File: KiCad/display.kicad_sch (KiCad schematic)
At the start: 36 parts, among them IC2 R1200N001A-TR-FE, J3 Conn_01x34_NHD_18, Q3 DMG2302U, U6 LT1963AxST-2.5

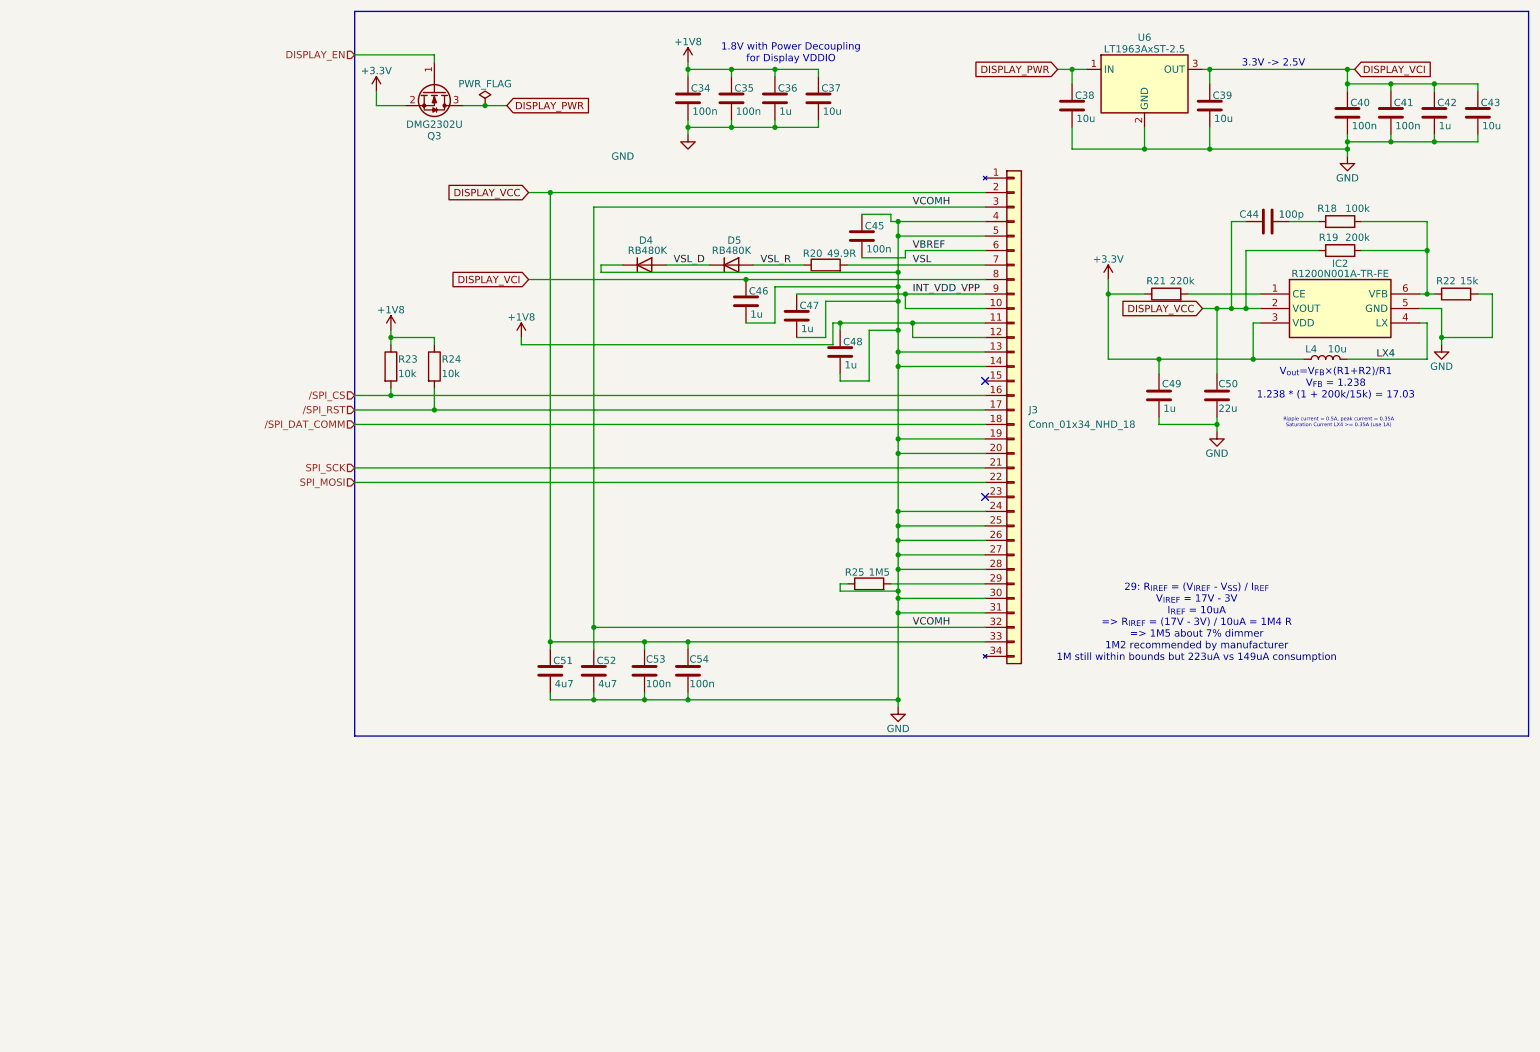
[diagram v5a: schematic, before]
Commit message: Organize components in power and display, setup PCB
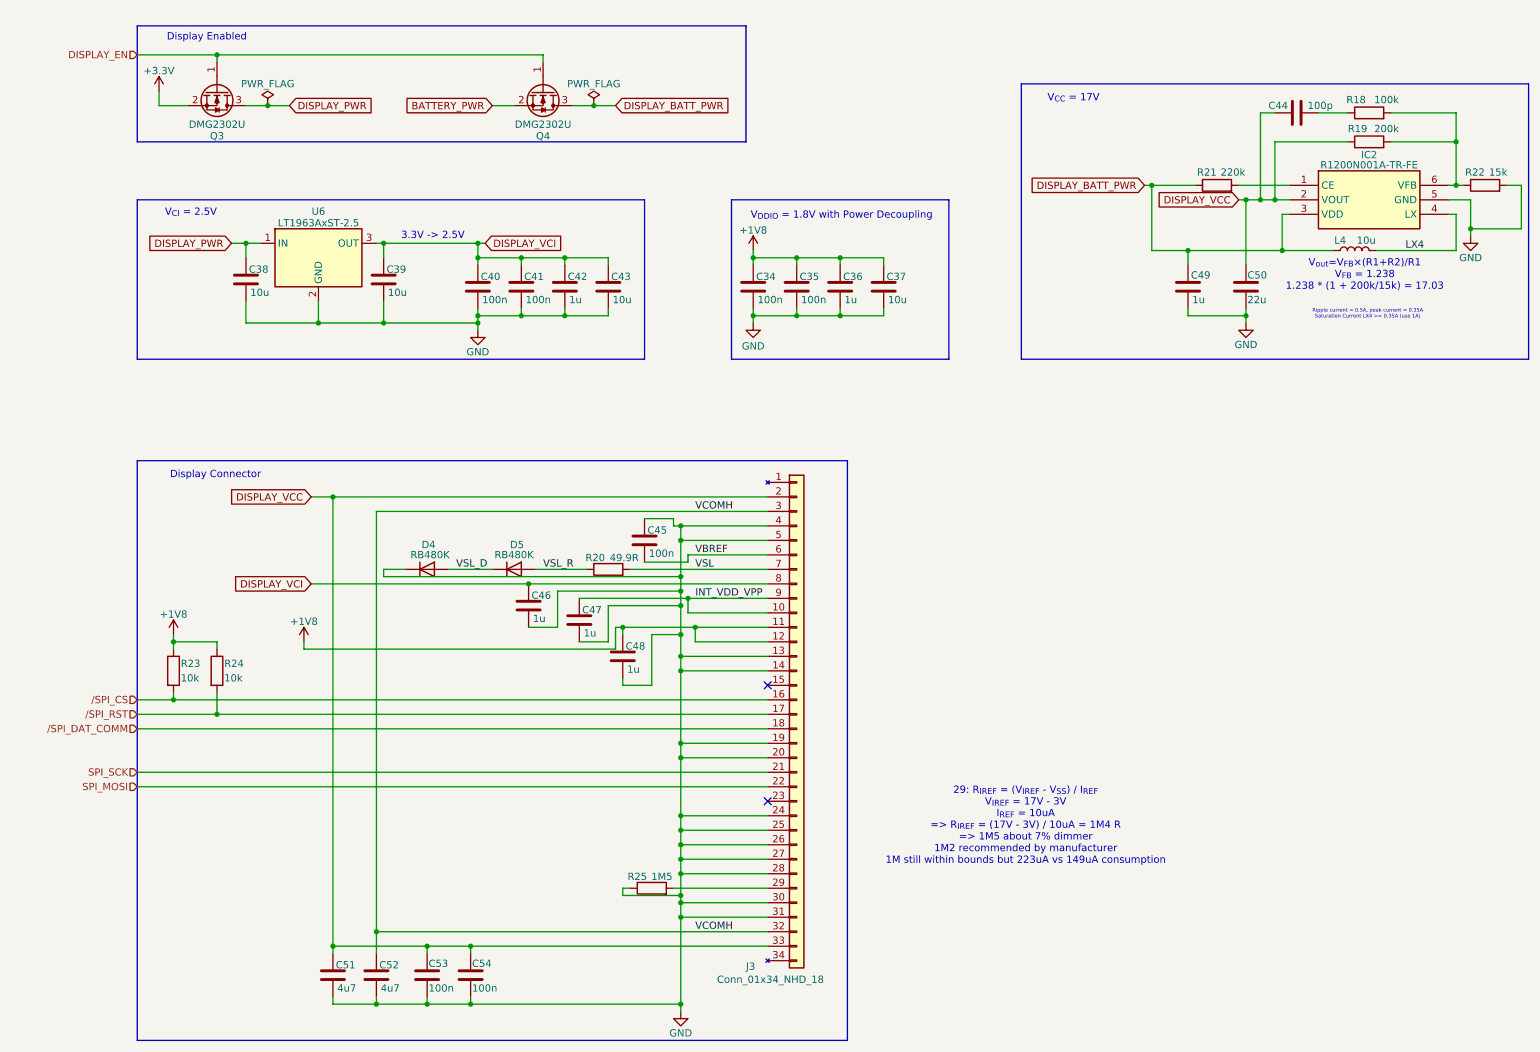
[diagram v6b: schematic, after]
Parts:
- added Q4: DMG2302U, Package_TO_SOT_SMD:SOT-23, symbol Transistor_FET:DMG2302U
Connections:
- net +3.3V: no longer C49.1, IC2.3 (VDD), L4.1, R21.1
- net DISPLAY_EN: now also Q4.1 (G)
- new net BATTERY_PWR: Q4.2 (S)
- new net DISPLAY_BATT_PWR: C49.1, IC2.3 (VDD), L4.1, Q4.3 (D), R21.1
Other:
- note added: "Display Connector"
- note added: "Display Enabled"
- note added: "V_{CC} = 17V"
- note added: "V_{CI} = 2.5V"
- note added: "V_{DDIO} = 1.8V with Power Decoupling"
- note removed: "1.8V with Power Decoupling for Display VDDIO"
- moved on the sheet: C34, C35, C36, C37, C38, C39, C40, C41, C42, C43, C44, C45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

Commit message: First Draft PCB Layout
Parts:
- removed C34, C35: 100n, Capacitor_SMD:C_0402_1005Metric, symbol Device:C
- removed C36, C46, C47: 1u, Capacitor_SMD:C_0402_1005Metric, symbol Device:C
- removed C37, C39: 10u, Capacitor_SMD:C_0402_1005Metric, symbol Device:C
- removed D4, D5: RB480K, Diode_SMD:D_SOD-323, symbol Device:D
- removed U6: LT1963AxST-2.5, Package_TO_SOT_SMD:SOT-223-3_TabPin2, symbol Regulator_Linear:LT1963AxST-2.5
- added C44, C45: 100n, Capacitor_SMD:C_0402_1005Metric, symbol Device:C
- added U6: MCP1700x-250xxTT, Package_TO_SOT_SMD:SOT-23, symbol Regulator_Linear:MCP1700x-250xxTT
- C38: renamed from C41; value 100n -> 1u
- renumbered C44 to C35, C38 to C36, C40 to C37, C42 to C39, C43 to C40, C49 to C41, C50 to C42, C45 to C43, C48 to C46, C51 to C47, C52 to C48, C53 to C49, C54 to C50, R21 to R20, R22 to R21, R20 to R22
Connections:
- net INT_VDD_VPP is gone; now on net DISPLAY_VCI: J3.10 (VDD), J3.9 (VPP=VDD)
- net +1V8: now also C44.1, C45.1
- net DISPLAY_VCC: now also R19.2; no longer R19.1
- net DISPLAY_VCI: now also U6.2 (VO)
- net GND: now also C44.2, C45.2, U6.1 (GND)
- net 17V_VFB: now reaches R18.1
- net 17V_VFB: now also IC2.6 (VFB), R19.1, R21.1; no longer C35.2
- net 17V_CE: now reaches IC2.1 (CE), R20.2
- net I_{REF}: now reaches J3.29 (IREF), R25.2
- net DISPLAY_PWR renamed DISPLAY_3V3
- net DISPLAY_3V3: now also U6.3 (VI)
- new net 17V_VFB_R: C35.2, R18.2
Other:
- note added: "Pin 8/9/10: Decoupling with Network in VCI section"
- note added: "RB480K replaced with the smaller footprint and active RB255ES-30"
- note removed: "V_{DDIO} = 1.8V with Power Decoupling"
- moved on the sheet: C35, R18, R19, R20

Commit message: Implement Comments, Working on PCB Layout
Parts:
- removed Q3, Q4: DMG2302U, Package_TO_SOT_SMD:SOT-23, symbol Transistor_FET:DMG2302U
- added D4, D5: RB522ES-30T15R, RB522ES-30T15R:RB522ES30, symbol RB522ES-30T15R:RB522ES-30T15R
- added IC1, IC2: TPS22916CNYFPR, TPS22916CNYFPR:BGA4C40P2X2_78X78X50, symbol TPS22916CNYFPR:TPS22916CNYFPR
- C37: renamed from C38; value 1u -> 100n
- renumbered C35 to C32, C41 to C33, C42 to C34, C36 to C35, C37 to C36, C39 to C38, C40 to C39, C43 to C40, C44 to C41, C45 to C42, C46 to C43, C47 to C44, C48 to C45, C49 to C46, C50 to C47, IC2 to IC3, R18 to R12, R19 to R13, R20 to R14, R21 to R15, R22 to R16, R23 to R17, R24 to R18, R25 to R19
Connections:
- net +3.3V: now also IC1.A2 (VIN)
- net DISPLAY_3V3: now also IC1.A1 (VOUT)
- net DISPLAY_BATT_PWR: now also IC2.A1 (VOUT)
- net DISPLAY_EN: now also IC1.B2 (ON), IC2.B2 (ON)
- net GND: now also D4.1 (K), IC1.B1 (GND), IC2.B1 (GND)
- net VSL_D: now also D4.2 (A), D5.1 (K)
- net VSL_R: now also D5.2 (A)
- new net SYS_PWR: IC2.A2 (VIN)
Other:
- note added: "Display PWR (ON/OFF)"
- note removed: "Display Enabled"
- note removed: "RB480K replaced with the smaller footprint and active RB255ES-30"
- moved on the sheet: C32, C33, C34, C35, C36, C37, C38, C39, C40, C41, C42, C43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
